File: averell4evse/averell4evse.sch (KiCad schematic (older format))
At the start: 31 parts, among them J1 Conn_01x16, J2 Conn_01x12, J3 Conn_01x04, U1 KT2520K-T, U2 NFCv4, U3 TLC5957RTQ, U4 74AUC1G126, U5 touch_sensor

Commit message: averell/sch: Swap test pad footprints from pad to plated hole
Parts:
- TP1, TP10, TP11, TP12, TP2, TP3, TP4, TP5, TP6, TP7, TP8, TP9: footprint TestPoint:TestPoint_Pad_1.0x1.0mm -> TestPoint:TestPoint_THTPad_D1.0mm_Drill0.5mm
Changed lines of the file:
@@
 F 0 "TP1" V 8250 3950 50  0000 C CNN
 F 1 "AUX1" V 8250 4200 50  0000 C CNN
-F 2 "TestPoint:TestPoint_Pad_1.0x1.0mm" H 8450 3700 50  0001 C CNN
+F 2 "TestPoint:TestPoint_THTPad_D1.0mm_Drill0.5mm" H 8450 3700 50  0001 C CNN
 F 3 "~" H 8450 3700 50  0001 C CNN
 	1    8250 3700
@@
 F 0 "TP2" V 8250 4050 50  0000 C CNN
 F 1 "AUX2" V 8250 4300 50  0000 C CNN
-F 2 "TestPoint:TestPoint_Pad_1.0x1.0mm" H 8450 3800 50  0001 C CNN
+F 2 "TestPoint:TestPoint_THTPad_D1.0mm_Drill0.5mm" H 8450 3800 50  0001 C CNN
 F 3 "~" H 8450 3800 50  0001 C CNN
 	1    8250 3800
@@
 F 0 "TP3" V 8250 4150 50  0000 C CNN
 F 1 "DBG_RXD" V 8250 4400 50  0000 C CNN
-F 2 "TestPoint:TestPoint_Pad_1.0x1.0mm" H 8450 3900 50  0001 C CNN
+F 2 "TestPoint:TestPoint_THTPad_D1.0mm_Drill0.5mm" H 8450 3900 50  0001 C CNN
 F 3 "~" H 8450 3900 50  0001 C CNN
 	1    8250 3900
@@
 F 0 "TP4" V 8250 4250 50  0000 C CNN
 F 1 "DBG_TXD" V 8250 4500 50  0000 C CNN
-F 2 "TestPoint:TestPoint_Pad_1.0x1.0mm" H 8450 4000 50  0001 C CNN
+F 2 "TestPoint:TestPoint_THTPad_D1.0mm_Drill0.5mm" H 8450 4000 50  0001 C CNN
 F 3 "~" H 8450 4000 50  0001 C CNN
 	1    8250 4000
@@
 F 0 "TP5" V 8250 4350 50  0000 C CNN
 F 1 "INT0" V 8250 4600 50  0000 C CNN
-F 2 "TestPoint:TestPoint_Pad_1.0x1.0mm" H 8450 4100 50  0001 C CNN
+F 2 "TestPoint:TestPoint_THTPad_D1.0mm_Drill0.5mm" H 8450 4100 50  0001 C CNN
 F 3 "~" H 8450 4100 50  0001 C CNN
 	1    8250 4100
@@
 F 0 "TP6" V 8250 4450 50  0000 C CNN
 F 1 "INT1" V 8250 4700 50  0000 C CNN
-F 2 "TestPoint:TestPoint_Pad_1.0x1.0mm" H 8450 4200 50  0001 C CNN
+F 2 "TestPoint:TestPoint_THTPad_D1.0mm_Drill0.5mm" H 8450 4200 50  0001 C CNN
 F 3 "~" H 8450 4200 50  0001 C CNN
 	1    8250 4200
@@
 F 0 "TP7" V 8250 4550 50  0000 C CNN
 F 1 "SIGCLK" V 8250 4800 50  0000 C CNN
-F 2 "TestPoint:TestPoint_Pad_1.0x1.0mm" H 8450 4300 50  0001 C CNN
+F 2 "TestPoint:TestPoint_THTPad_D1.0mm_Drill0.5mm" H 8450 4300 50  0001 C CNN
 F 3 "~" H 8450 4300 50  0001 C CNN
 	1    8250 4300
@@
 F 0 "TP8" V 8250 4650 50  0000 C CNN
 F 1 "SIGOUT" V 8250 4900 50  0000 C CNN
-F 2 "TestPoint:TestPoint_Pad_1.0x1.0mm" H 8450 4400 50  0001 C CNN
+F 2 "TestPoint:TestPoint_THTPad_D1.0mm_Drill0.5mm" H 8450 4400 50  0001 C CNN
 F 3 "~" H 8450 4400 50  0001 C CNN
 	1    8250 4400
@@
 F 0 "TP9" V 8250 4750 50  0000 C CNN
 F 1 "SIGIN" V 8250 5000 50  0000 C CNN
-F 2 "TestPoint:TestPoint_Pad_1.0x1.0mm" H 8450 4500 50  0001 C CNN
+F 2 "TestPoint:TestPoint_THTPad_D1.0mm_Drill0.5mm" H 8450 4500 50  0001 C CNN
 F 3 "~" H 8450 4500 50  0001 C CNN
 	1    8250 4500
@@
 F 0 "TP10" V 5300 6300 50  0000 C CNN
 F 1 "R13" V 5300 6550 50  0000 C CNN
-F 2 "TestPoint:TestPoint_Pad_1.0x1.0mm" H 5500 6050 50  0001 C CNN
+F 2 "TestPoint:TestPoint_THTPad_D1.0mm_Drill0.5mm" H 5500 6050 50  0001 C CNN
 F 3 "~" H 5500 6050 50  0001 C CNN
 	1    5300 6050
@@
 F 0 "TP11" V 5300 6400 50  0000 C CNN
 F 1 "G13" V 5300 6650 50  0000 C CNN
-F 2 "TestPoint:TestPoint_Pad_1.0x1.0mm" H 5500 6150 50  0001 C CNN
+F 2 "TestPoint:TestPoint_THTPad_D1.0mm_Drill0.5mm" H 5500 6150 50  0001 C CNN
 F 3 "~" H 5500 6150 50  0001 C CNN
 	1    5300 6150
@@
 F 0 "TP12" V 5300 6500 50  0000 C CNN
 F 1 "B13" V 5300 6750 50  0000 C CNN
-F 2 "TestPoint:TestPoint_Pad_1.0x1.0mm" H 5500 6250 50  0001 C CNN
+F 2 "TestPoint:TestPoint_THTPad_D1.0mm_Drill0.5mm" H 5500 6250 50  0001 C CNN
 F 3 "~" H 5500 6250 50  0001 C CNN
 	1    5300 6250

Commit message: averell/*: Update LED footprint with custom internal one
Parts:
- D1, D2, D3, D4, D5, D6, D7, D8: footprint LED_SMD:LED_Avago_PLCC4_3.2x2.8mm_CW -> ma4evse:LED_Avago_PLCC4_3.2x2.8mm_CW
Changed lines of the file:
@@
 F 0 "D1" H 6050 1667 50  0000 C CNN
 F 1 "ASMB-MTB0-0A3A2" H 6050 1576 50  0000 C CNN
-F 2 "LED_SMD:LED_Avago_PLCC4_3.2x2.8mm_CW" H 6050 1650 50  0001 C CNN
+F 2 "ma4evse:LED_Avago_PLCC4_3.2x2.8mm_CW" H 6050 1650 50  0001 C CNN
 F 3 "https://docs.broadcom.com/docs/AV02-4186EN" H 6050 700 50  0001 C CNN
 	1    6050 1150
@@
 F 0 "D2" H 7000 1667 50  0000 C CNN
 F 1 "ASMB-MTB0-0A3A2" H 7000 1576 50  0000 C CNN
-F 2 "LED_SMD:LED_Avago_PLCC4_3.2x2.8mm_CW" H 7000 1650 50  0001 C CNN
+F 2 "ma4evse:LED_Avago_PLCC4_3.2x2.8mm_CW" H 7000 1650 50  0001 C CNN
 F 3 "https://docs.broadcom.com/docs/AV02-4186EN" H 7000 700 50  0001 C CNN
 	1    7000 1150
@@
 F 0 "D3" H 7950 1667 50  0000 C CNN
 F 1 "ASMB-MTB0-0A3A2" H 7950 1576 50  0000 C CNN
-F 2 "LED_SMD:LED_Avago_PLCC4_3.2x2.8mm_CW" H 7950 1650 50  0001 C CNN
+F 2 "ma4evse:LED_Avago_PLCC4_3.2x2.8mm_CW" H 7950 1650 50  0001 C CNN
 F 3 "https://docs.broadcom.com/docs/AV02-4186EN" H 7950 700 50  0001 C CNN
 	1    7950 1150
@@
 F 0 "D4" H 8900 1667 50  0000 C CNN
 F 1 "ASMB-MTB0-0A3A2" H 8900 1576 50  0000 C CNN
-F 2 "LED_SMD:LED_Avago_PLCC4_3.2x2.8mm_CW" H 8900 1650 50  0001 C CNN
+F 2 "ma4evse:LED_Avago_PLCC4_3.2x2.8mm_CW" H 8900 1650 50  0001 C CNN
 F 3 "https://docs.broadcom.com/docs/AV02-4186EN" H 8900 700 50  0001 C CNN
 	1    8900 1150
@@
 F 0 "D5" H 6050 2767 50  0000 C CNN
 F 1 "ASMB-MTB0-0A3A2" H 6050 2676 50  0000 C CNN
-F 2 "LED_SMD:LED_Avago_PLCC4_3.2x2.8mm_CW" H 6050 2750 50  0001 C CNN
+F 2 "ma4evse:LED_Avago_PLCC4_3.2x2.8mm_CW" H 6050 2750 50  0001 C CNN
 F 3 "https://docs.broadcom.com/docs/AV02-4186EN" H 6050 1800 50  0001 C CNN
 	1    6050 2250
@@
 F 0 "D6" H 7000 2767 50  0000 C CNN
 F 1 "ASMB-MTB0-0A3A2" H 7000 2676 50  0000 C CNN
-F 2 "LED_SMD:LED_Avago_PLCC4_3.2x2.8mm_CW" H 7000 2750 50  0001 C CNN
+F 2 "ma4evse:LED_Avago_PLCC4_3.2x2.8mm_CW" H 7000 2750 50  0001 C CNN
 F 3 "https://docs.broadcom.com/docs/AV02-4186EN" H 7000 1800 50  0001 C CNN
 	1    7000 2250
@@
 F 0 "D7" H 7950 2767 50  0000 C CNN
 F 1 "ASMB-MTB0-0A3A2" H 7950 2676 50  0000 C CNN
-F 2 "LED_SMD:LED_Avago_PLCC4_3.2x2.8mm_CW" H 7950 2750 50  0001 C CNN
+F 2 "ma4evse:LED_Avago_PLCC4_3.2x2.8mm_CW" H 7950 2750 50  0001 C CNN
 F 3 "https://docs.broadcom.com/docs/AV02-4186EN" H 7950 1800 50  0001 C CNN
 	1    7950 2250
@@
 F 0 "D8" H 8900 2767 50  0000 C CNN
 F 1 "ASMB-MTB0-0A3A2" H 8900 2676 50  0000 C CNN
-F 2 "LED_SMD:LED_Avago_PLCC4_3.2x2.8mm_CW" H 8900 2750 50  0001 C CNN
+F 2 "ma4evse:LED_Avago_PLCC4_3.2x2.8mm_CW" H 8900 2750 50  0001 C CNN
 F 3 "https://docs.broadcom.com/docs/AV02-4186EN" H 8900 1800 50  0001 C CNN
 	1    8900 2250

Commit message: averell/sch: Use mirrored NFCv4 footprint
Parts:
- U2: footprint ma4evse:nfc_v4 -> ma4evse:nfc_v4_mirror
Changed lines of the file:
@@
 F 0 "U2" H 6900 3750 50  0000 C CNN
 F 1 "NFCv4" H 6950 3650 50  0000 C CNN
-F 2 "ma4evse:nfc_v4" H 6850 3600 50  0001 C CNN
+F 2 "ma4evse:nfc_v4_mirror" H 6850 3600 50  0001 C CNN
 F 3 "http://www.elechouse.com/elechouse/images/product/PN532_module_V3/PN532_%20Manual_V3.pdf" H 6850 3600 50  0001 C CNN
 	1    6850 3600

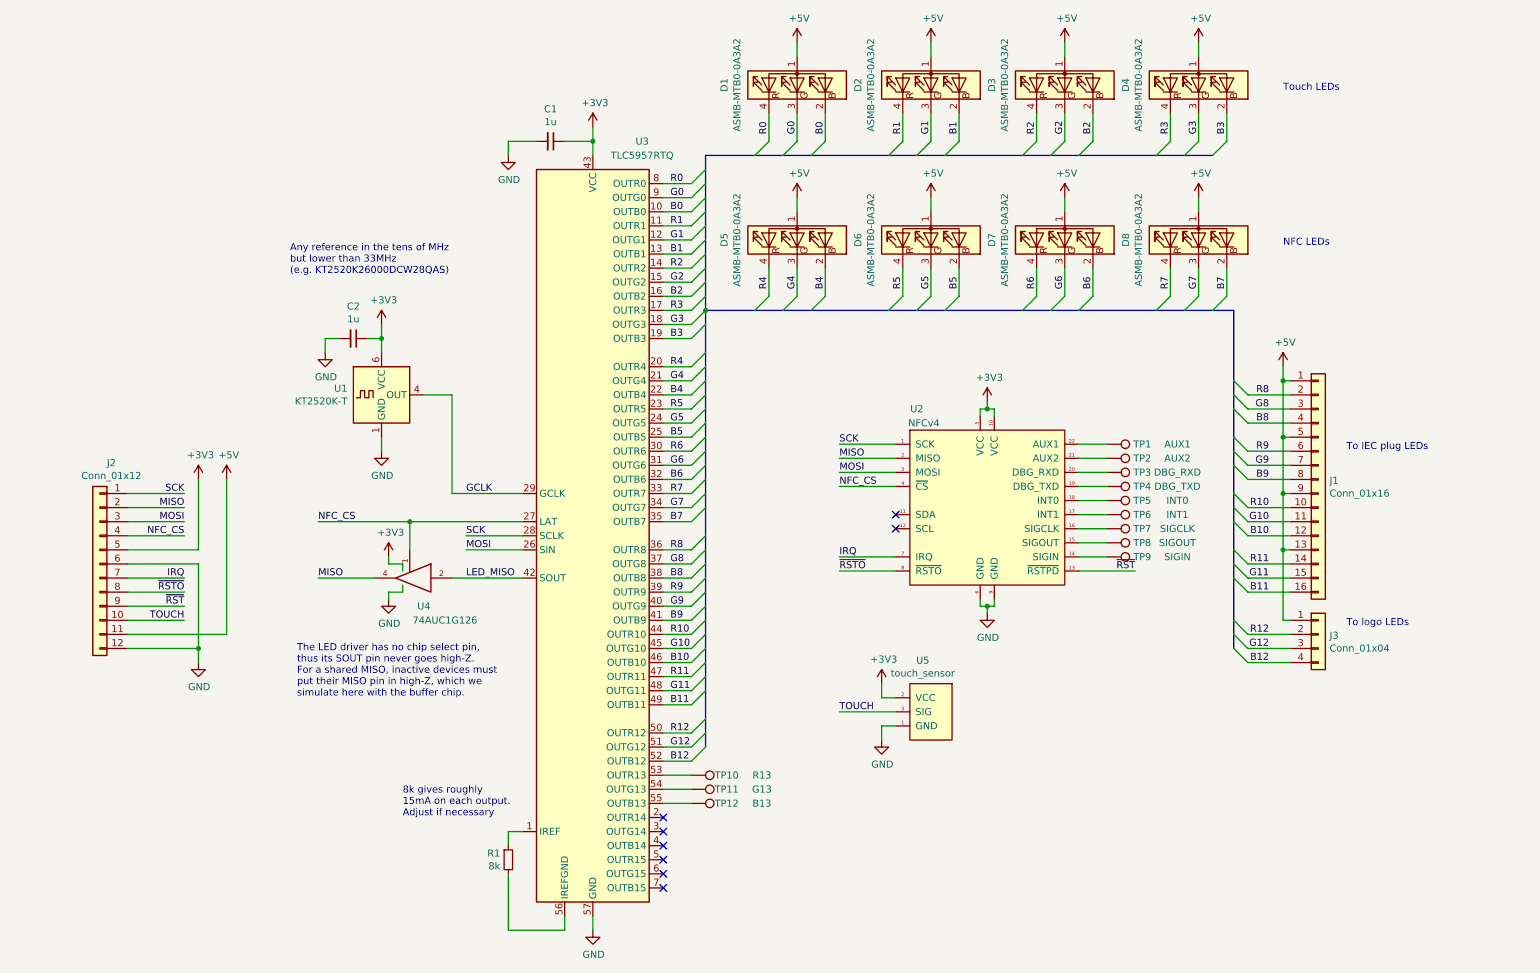
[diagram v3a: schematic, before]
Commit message: averell/sch: Put 3 LEDs per channel rather than one
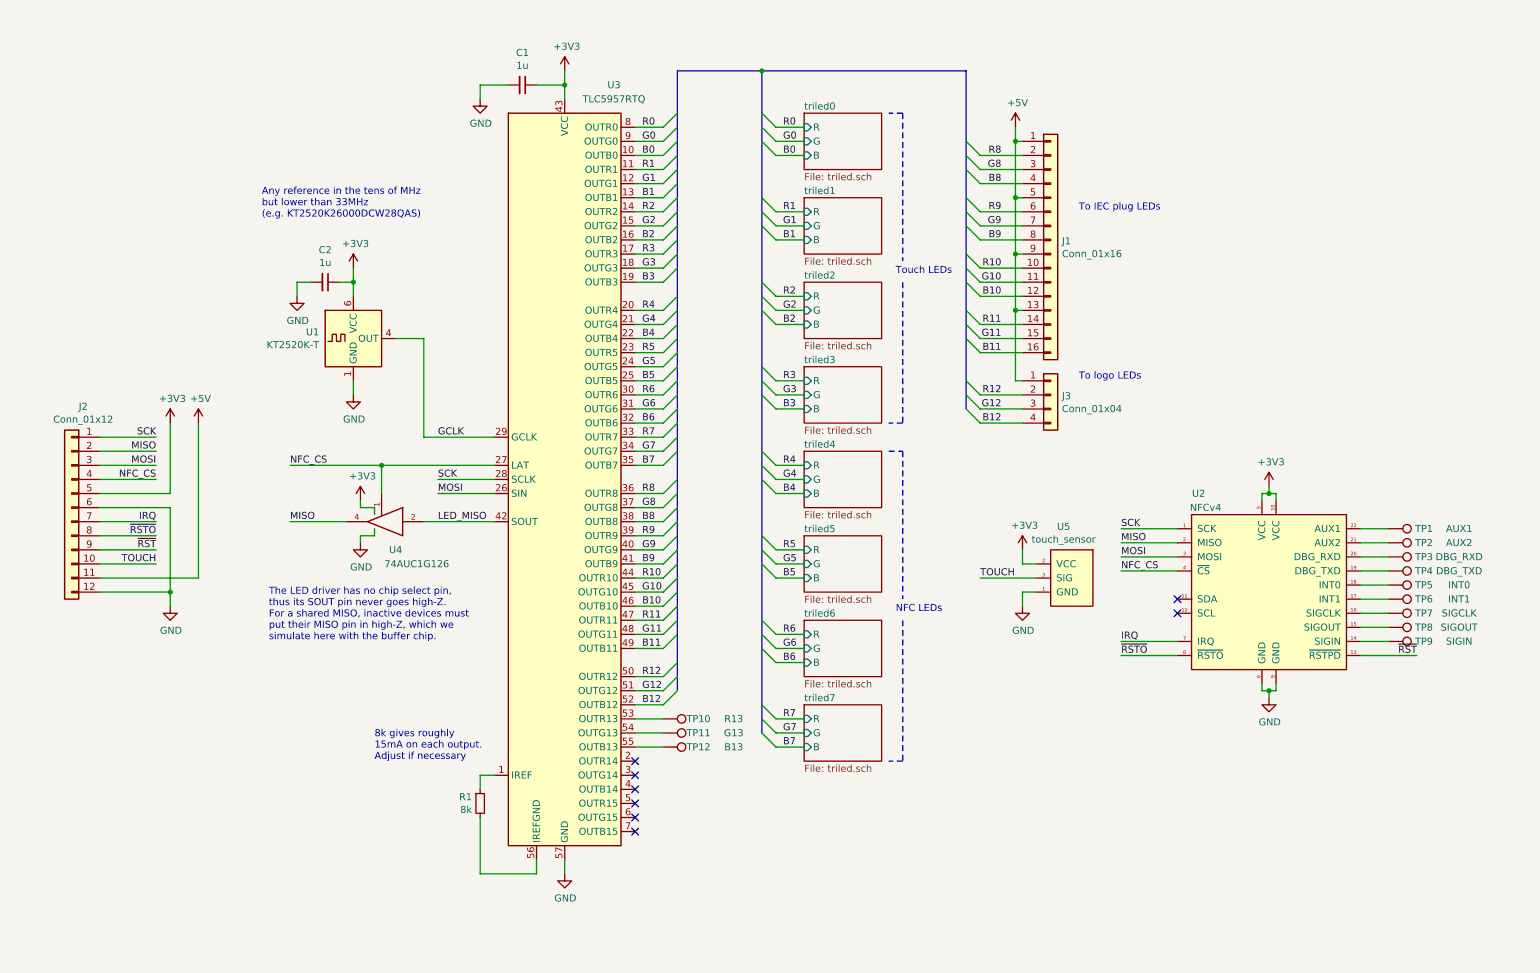
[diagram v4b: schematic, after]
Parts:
- removed D1, D2, D3, D4, D5, D6, D7, D8: ASMB-MTB0-0A3A2, ma4evse:LED_Avago_PLCC4_3.2x2.8mm_CW, symbol LED:ASMB-MTB0-0A3A2
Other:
- moved on the sheet: C1, C2, J1, J2, J3, R1, TP1, TP10, TP11, TP12, TP2, TP3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

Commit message: averell/sch: Add power flags to make ERC happy
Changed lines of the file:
@@
 	5800 1050 7250 1050
 Connection ~ 5800 1050
+$Comp
+L power:PWR_FLAG #FLG0101
+U 1 1 5E51A4BC
+P 1100 1500
+F 0 "#FLG0101" H 1100 1575 50  0001 C CNN
+F 1 "PWR_FLAG" H 1100 1673 50  0000 C CNN
+F 2 "" H 1100 1500 50  0001 C CNN
+F 3 "~" H 1100 1500 50  0001 C CNN
+	1    1100 1500
+	1    0    0    -1
+$EndComp
+$Comp
+L power:PWR_FLAG #FLG0102
+U 1 1 5E51BAB0
+P 900 1050
+F 0 "#FLG0102" H 900 1125 50  0001 C CNN
+F 1 "PWR_FLAG" H 900 1223 50  0000 C CNN
+F 2 "" H 900 1050 50  0001 C CNN
+F 3 "~" H 900 1050 50  0001 C CNN
+	1    900  1050
+	-1   0    0    1
+$EndComp
+$Comp
+L power:PWR_FLAG #FLG0103
+U 1 1 5E526024
+P 1300 1050
+F 0 "#FLG0103" H 1300 1125 50  0001 C CNN
+F 1 "PWR_FLAG" H 1300 1223 50  0000 C CNN
+F 2 "" H 1300 1050 50  0001 C CNN
+F 3 "~" H 1300 1050 50  0001 C CNN
+	1    1300 1050
+	-1   0    0    1
+$EndComp
+$Comp
+L power:+3V3 #PWR0113
+U 1 1 5E5261F7
+P 900 1050
+F 0 "#PWR0113" H 900 900 50  0001 C CNN
+F 1 "+3V3" H 915 1223 50  0000 C CNN
+F 2 "" H 900 1050 50  0001 C CNN
+F 3 "" H 900 1050 50  0001 C CNN
+	1    900  1050
+	1    0    0    -1
+$EndComp
+$Comp
+L power:+5V #PWR0114
+U 1 1 5E526AB8
+P 1300 1050
+F 0 "#PWR0114" H 1300 900 50  0001 C CNN
+F 1 "+5V" H 1315 1223 50  0000 C CNN
+F 2 "" H 1300 1050 50  0001 C CNN
+F 3 "" H 1300 1050 50  0001 C CNN
+	1    1300 1050
+	1    0    0    -1
+$EndComp
+$Comp
+L power:GND #PWR0115
+U 1 1 5E526FE2
+P 1100 1500
+F 0 "#PWR0115" H 1100 1250 50  0001 C CNN
+F 1 "GND" H 1105 1327 50  0000 C CNN
+F 2 "" H 1100 1500 50  0001 C CNN
+F 3 "" H 1100 1500 50  0001 C CNN
+	1    1100 1500
+	1    0    0    -1
+$EndComp
 Wire Bus Line
 	7250 1050 7250 3450
